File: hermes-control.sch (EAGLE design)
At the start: 74 parts, among them J1 1981568-1, J3 2201778-1, Q2 BC849SMD, Q3 FDN360P, Q4 FDN360P, Q5 BC849SMD, Q6 MMBT3906SOT23-3, Q7 FDN360P, Q8 MMBT2222A, U1 LSM9DS1TR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

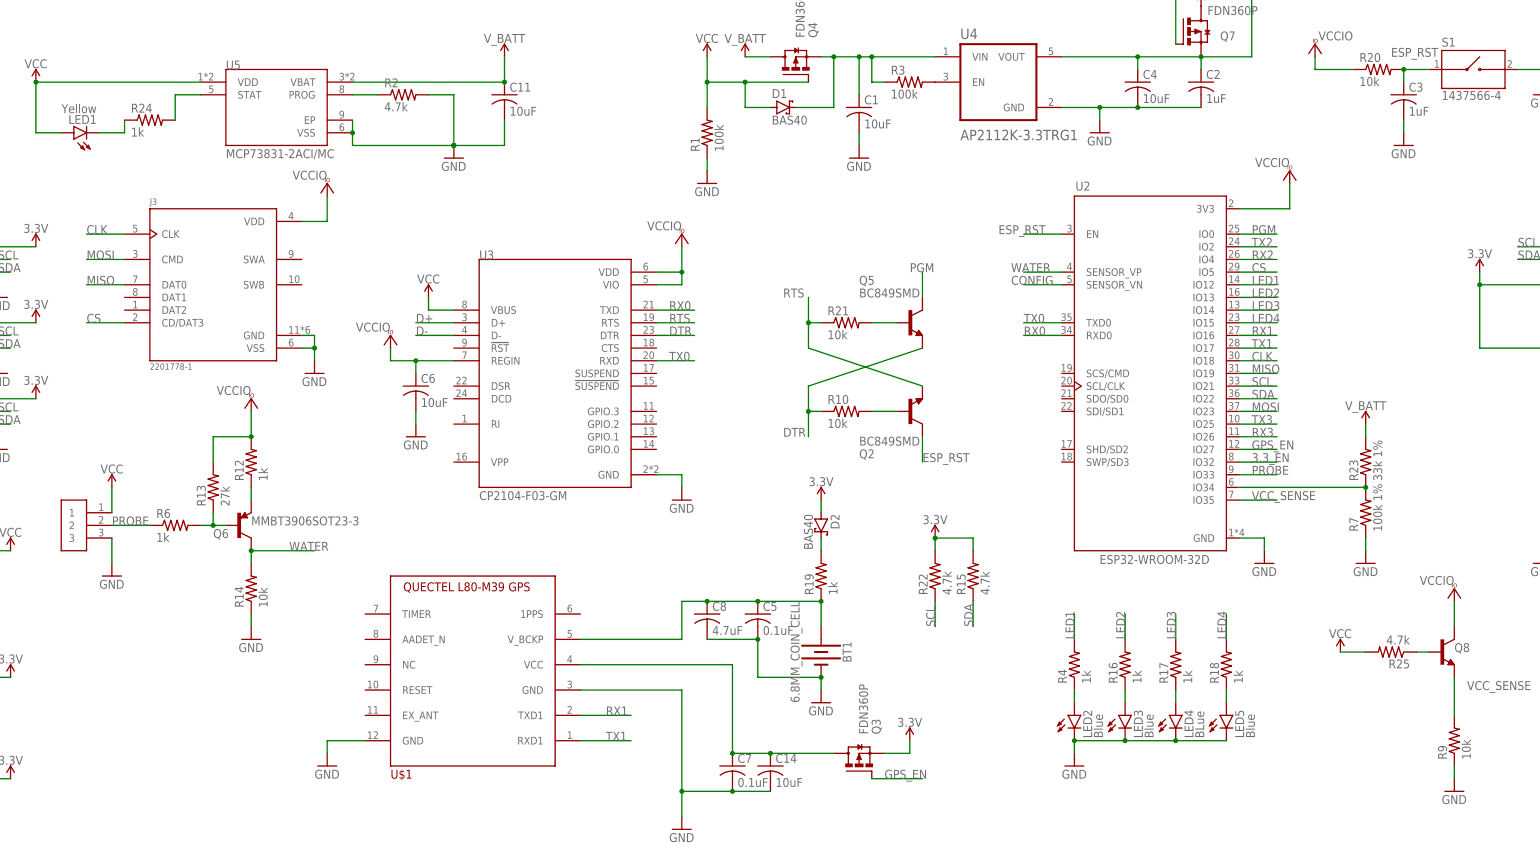
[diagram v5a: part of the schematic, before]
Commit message: Answers to Questions: - ESP32_RST looks like it should be a 0.1uF not 1uF (p15)  -- fixed - similarly, the reference decoupling caps for 3V3 (pin 2) are 10uF and 0.1uF but you have 10uF and 1uF (on VCCIO)  -- fixed - for the L80, I don't see a pull-up on GPS_EN -- does GPIO27 have an internal pull-up? (for pFET to cut main power to GPS when ESP32 sleeps)  -- fixed - on the LSM the bridging of VDD and VDDIO raises the question of how the decoupling will interact.  -- not a problem - we're just holding VDD_IO high by matching it to supply (VDD), no filtering actually needed
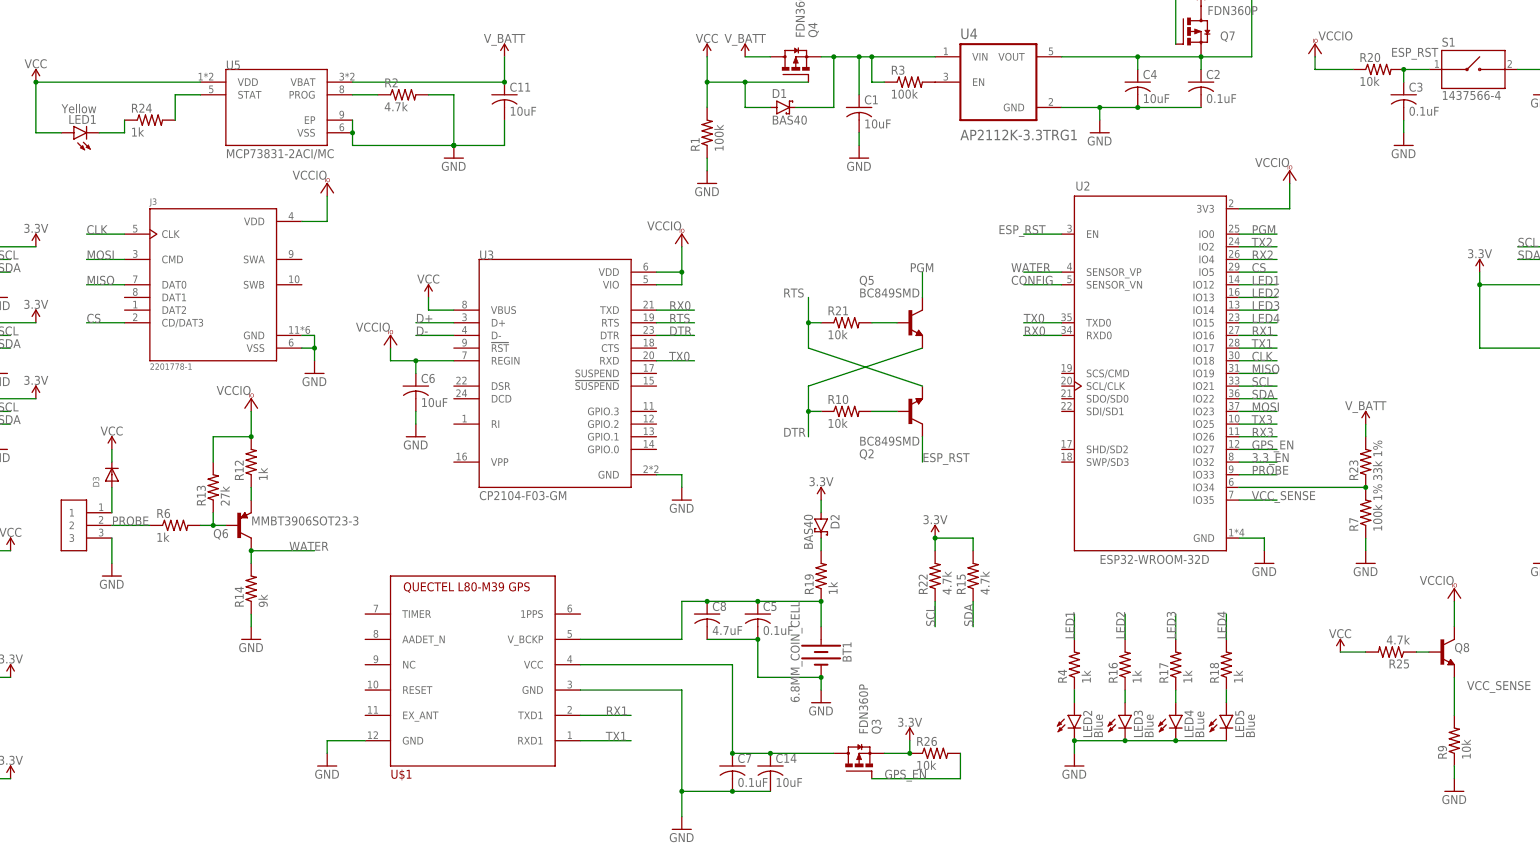
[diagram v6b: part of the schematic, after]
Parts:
- added D3: (no value), adafruit:DIODE_SOD-123FL
- added R26: 10k, rcl:R-US_R0603
- C2, C3: value 1uF -> 0.1uF
- R14: value 10k -> 9k
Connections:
- new net N$7: D3.A, U$2.1
- net 3.3V: now also R26.1
- net GPS_EN: now also R26.2
- net VCC: now also D3.C; no longer U$2.1
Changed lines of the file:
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@@
 <part name="R3" library="rcl" library_urn="urn:adsk.eagle:library:334" deviceset="R-US_" device="R0603" package3d_urn="urn:adsk.eagle:package:23555/3" value="100k"/>
 <part name="C4" library="rcl" library_urn="urn:adsk.eagle:library:334" deviceset="C-US" device="C0603" package3d_urn="urn:adsk.eagle:package:23616/2" value="10uF"/>
-<part name="C2" library="rcl" library_urn="urn:adsk.eagle:library:334" deviceset="C-US" device="C0603" package3d_urn="urn:adsk.eagle:package:23616/2" value="1uF"/>
-<part name="C3" library="rcl" library_urn="urn:adsk.eagle:library:334" deviceset="C-US" device="C0603" package3d_urn="urn:adsk.eagle:package:23616/2" value="1uF"/>
+<part name="C2" library="rcl" library_urn="urn:adsk.eagle:library:334" deviceset="C-US" device="C0603" package3d_urn="urn:adsk.eagle:package:23616/2" value="0.1uF"/>
+<part name="C3" library="rcl" library_urn="urn:adsk.eagle:library:334" deviceset="C-US" device="C0603" package3d_urn="urn:adsk.eagle:package:23616/2" value="0.1uF"/>
 <part name="C10" library="rcl" library_urn="urn:adsk.eagle:library:334" deviceset="C-US" device="C0603" package3d_urn="urn:adsk.eagle:package:23616/2" value="10uF"/>
 <part name="C12" library="rcl" library_urn="urn:adsk.eagle:library:334" deviceset="C-US" device="C0603" package3d_urn="urn:adsk.eagle:package:23616/2" value="0.1uF"/>
@@
 <part name="R12" library="rcl" library_urn="urn:adsk.eagle:library:334" deviceset="R-US_" device="R0603" package3d_urn="urn:adsk.eagle:package:23555/3" value="1k"/>
 <part name="R13" library="rcl" library_urn="urn:adsk.eagle:library:334" deviceset="R-US_" device="R0603" package3d_urn="urn:adsk.eagle:package:23555/3" value="27k"/>
-<part name="R14" library="rcl" library_urn="urn:adsk.eagle:library:334" deviceset="R-US_" device="R0603" package3d_urn="urn:adsk.eagle:package:23555/3" value="10k"/>
+<part name="R14" library="rcl" library_urn="urn:adsk.eagle:library:334" deviceset="R-US_" device="R0603" package3d_urn="urn:adsk.eagle:package:23555/3" value="9k"/>
 <part name="GND28" library="supply1" library_urn="urn:adsk.eagle:library:371" deviceset="GND" device=""/>
 <part name="U$2" library="BlueRobotics-JST-GH" deviceset="JST-GH-3" device="VERT"/>
@@
 <part name="VCC9" library="supply1" library_urn="urn:adsk.eagle:library:371" deviceset="VCCIO" device=""/>
 <part name="R5" library="rcl" library_urn="urn:adsk.eagle:library:334" deviceset="R-US_" device="R0603" package3d_urn="urn:adsk.eagle:package:23555/3" value="10k"/>
+<part name="R26" library="rcl" library_urn="urn:adsk.eagle:library:334" deviceset="R-US_" device="R0603" package3d_urn="urn:adsk.eagle:package:23555/3" value="10k"/>
+<part name="D3" library="adafruit" library_urn="urn:adsk.eagle:library:420" deviceset="DIODE" device="_SOD-123FL" package3d_urn="urn:adsk.eagle:package:6240937/1"/>
 </parts>
 <sheets>
@@
 <attribute name="VALUE" x="83.82" y="66.04" size="1.778" layer="96"/>
 </instance>
-<instance part="SUPPLY27" gate="G$1" x="86.36" y="86.36" smashed="yes">
-<attribute name="VALUE" x="86.36" y="89.154" size="1.778" layer="96" align="bottom-center"/>
+<instance part="SUPPLY27" gate="G$1" x="86.36" y="93.98" smashed="yes">
+<attribute name="VALUE" x="86.36" y="96.774" size="1.778" layer="96" align="bottom-center"/>
 </instance>
 <instance part="C9" gate="G$1" x="421.64" y="101.6" smashed="yes">
@@
 <attribute name="NAME" x="300.99" y="191.9986" size="1.778" layer="95"/>
 <attribute name="VALUE" x="300.99" y="187.198" size="1.778" layer="96"/>
+</instance>
+<instance part="R26" gate="G$1" x="251.46" y="33.02" smashed="yes">
+<attribute name="NAME" x="247.65" y="34.5186" size="1.778" layer="95"/>
+<attribute name="VALUE" x="247.65" y="29.718" size="1.778" layer="96"/>
+</instance>
+<instance part="D3" gate="G$1" x="86.36" y="88.9" smashed="yes" rot="R90">
+<attribute name="NAME" x="83.82" y="86.36" size="1.27" layer="95" rot="R90"/>
+<attribute name="VALUE" x="90.17" y="86.36" size="1.27" layer="96" rot="R90"/>
 </instance>
 </instances>
@@
 </segment>
 <segment>
-<pinref part="U$2" gate="G$1" pin="1"/>
-<pinref part="SUPPLY27" gate="G$1" pin="VCC"/>
-<wire x1="86.36" y1="81.28" x2="86.36" y2="86.36" width="0.1524" layer="91"/>
-</segment>
-<segment>
 <pinref part="SUPPLY30" gate="G$1" pin="VCC"/>
 <pinref part="R25" gate="G$1" pin="2"/>
@@
 <wire x1="149.86" y1="121.92" x2="149.86" y2="124.46" width="0.1524" layer="91"/>
 </segment>
+<segment>
+<pinref part="D3" gate="G$1" pin="C"/>
+<pinref part="SUPPLY27" gate="G$1" pin="VCC"/>
+<wire x1="86.36" y1="91.44" x2="86.36" y2="93.98" width="0.1524" layer="91"/>
+</segment>
 </net>
 <net name="N$2" class="0">
@@
 <pinref part="Q3" gate="G$1" pin="S"/>
 <wire x1="241.3" y1="33.02" x2="246.38" y2="33.02" width="0.1524" layer="91"/>
+<pinref part="R26" gate="G$1" pin="1"/>
+<junction x="246.38" y="33.02"/>
 </segment>
 <segment>
@@
 </segment>
 <segment>
-<wire x1="238.76" y1="27.94" x2="248.92" y2="27.94" width="0.1524" layer="91"/>
+<wire x1="238.76" y1="27.94" x2="256.54" y2="27.94" width="0.1524" layer="91"/>
 <label x="241.3" y="27.94" size="1.778" layer="95"/>
 <pinref part="Q3" gate="G$1" pin="G"/>
+<pinref part="R26" gate="G$1" pin="2"/>
+<wire x1="256.54" y1="33.02" x2="256.54" y2="27.94" width="0.1524" layer="91"/>
 </segment>
 </net>
@@
 </segment>
 </net>
+<net name="N$7" class="0">
+<segment>
+<pinref part="U$2" gate="G$1" pin="1"/>
+<pinref part="D3" gate="G$1" pin="A"/>
+<wire x1="86.36" y1="81.28" x2="86.36" y2="86.36" width="0.1524" layer="91"/>
+</segment>
+</net>

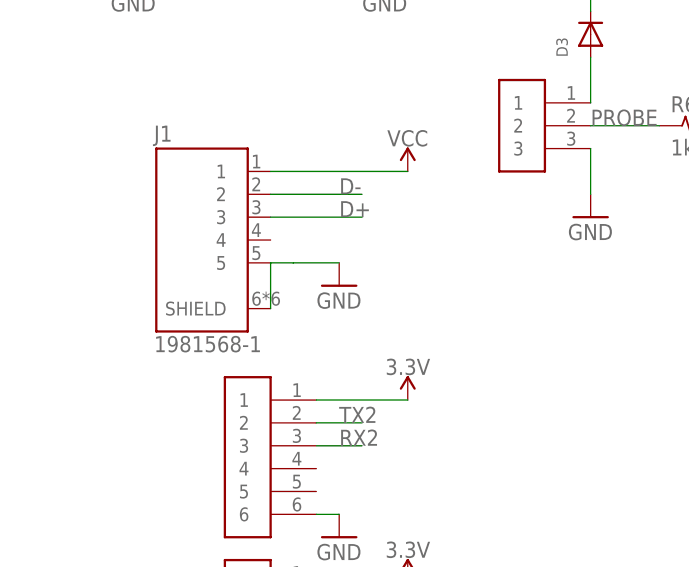
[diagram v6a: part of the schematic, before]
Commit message: Change silkscreen back to Remora and clean up lots of small things.
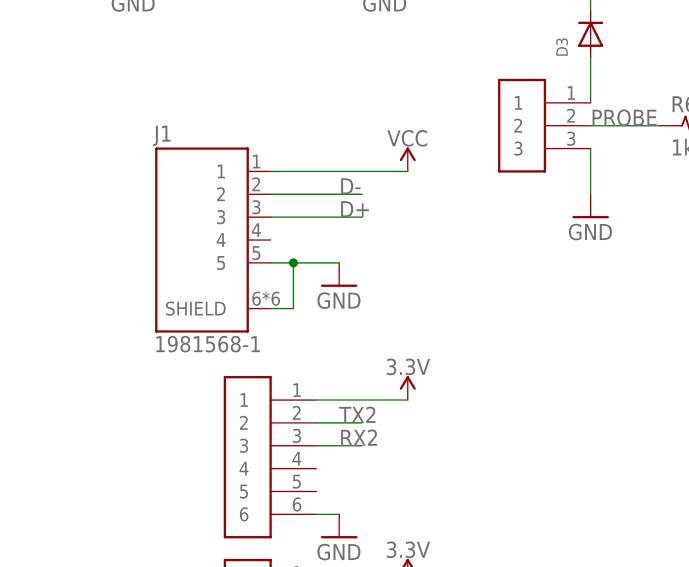
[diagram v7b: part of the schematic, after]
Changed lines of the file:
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@@
 <?xml version="1.0" encoding="utf-8"?>
 <!DOCTYPE eagle SYSTEM "eagle.dtd">
-<eagle version="9.3.0">
+<eagle version="9.4.0">
 <drawing>
 <settings>
-<setting alwaysvectorfont="no"/>
+<setting alwaysvectorfont="yes"/>
 <setting verticaltext="up"/>
 </settings>
@@
 <pinref part="J1" gate="G$1" pin="SHIELD"/>
 <wire x1="53.34" y1="63.5" x2="50.8" y2="63.5" width="0.1524" layer="91"/>
-<wire x1="50.8" y1="63.5" x2="50.8" y2="58.42" width="0.1524" layer="91"/>
-</segment>
-<segment>
+<wire x1="50.8" y1="58.42" x2="53.34" y2="58.42" width="0.1524" layer="91"/>
+<wire x1="53.34" y1="58.42" x2="53.34" y2="63.5" width="0.1524" layer="91"/>
+<junction x="53.34" y="63.5"/>
+</segment>
+<segment>
